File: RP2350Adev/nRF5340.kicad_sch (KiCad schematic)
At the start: 20 parts, among them J1 J-Link, J3 Conn_01x04, U2 nRF5340-QKxx, X1 32.768kHz, X2 32MHz

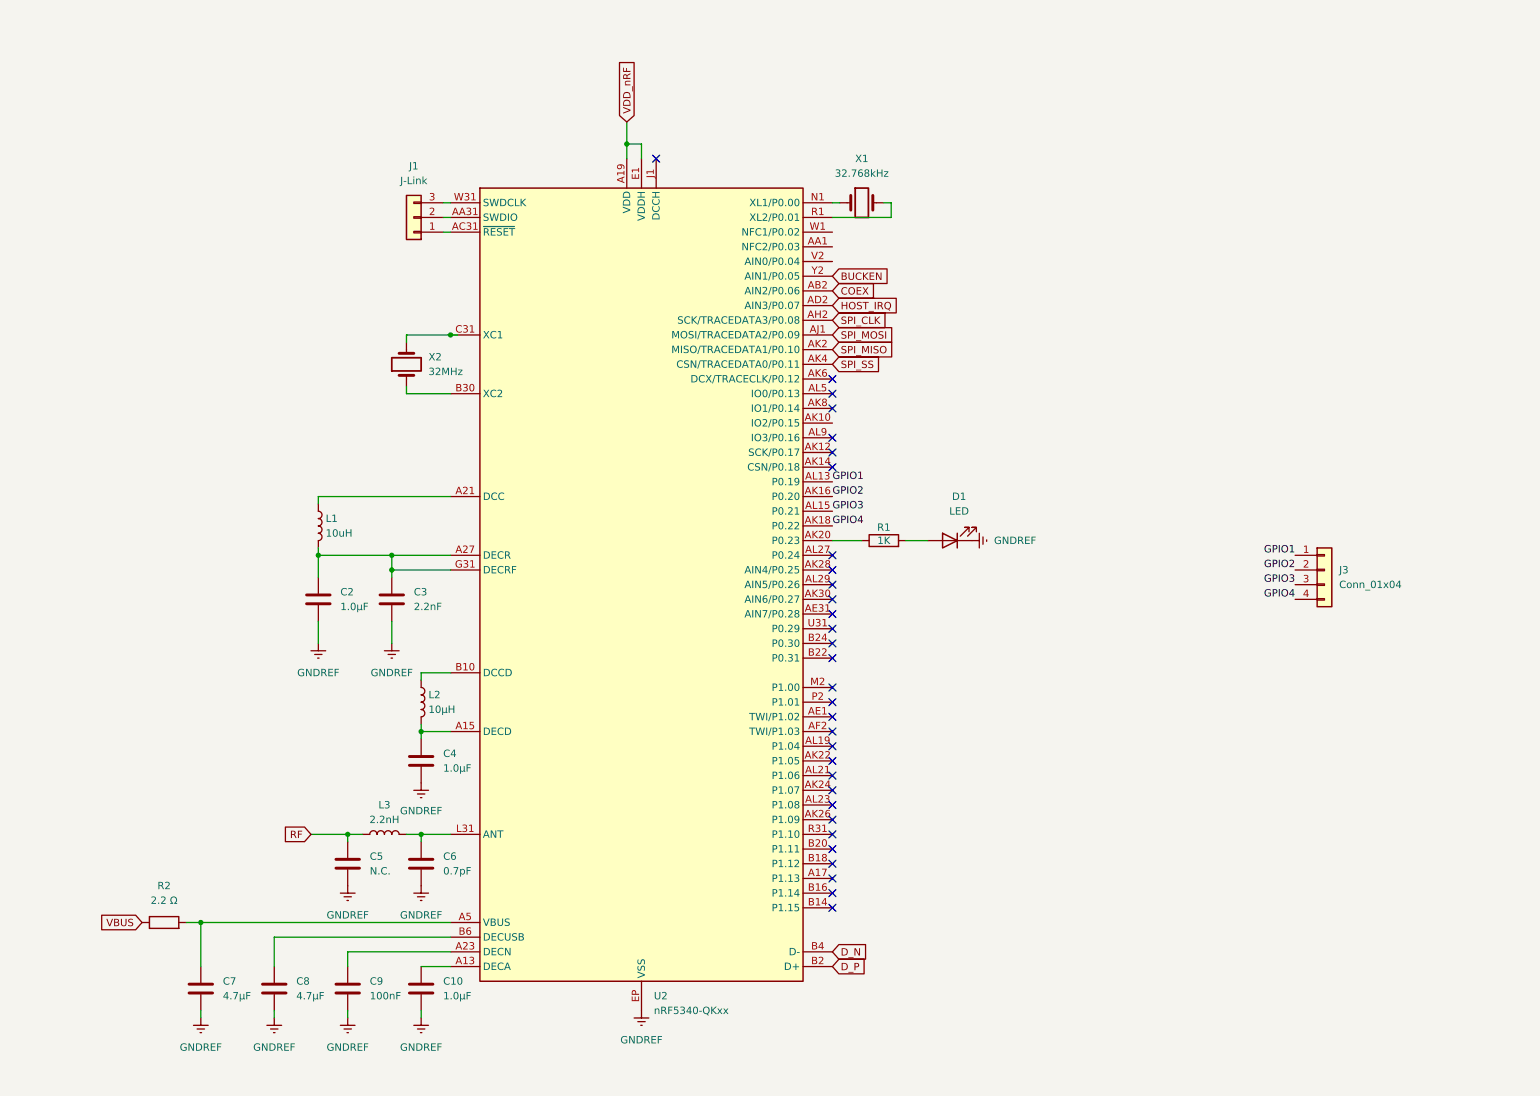
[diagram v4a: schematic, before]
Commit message: Updated nRF5340 with footprints and labels
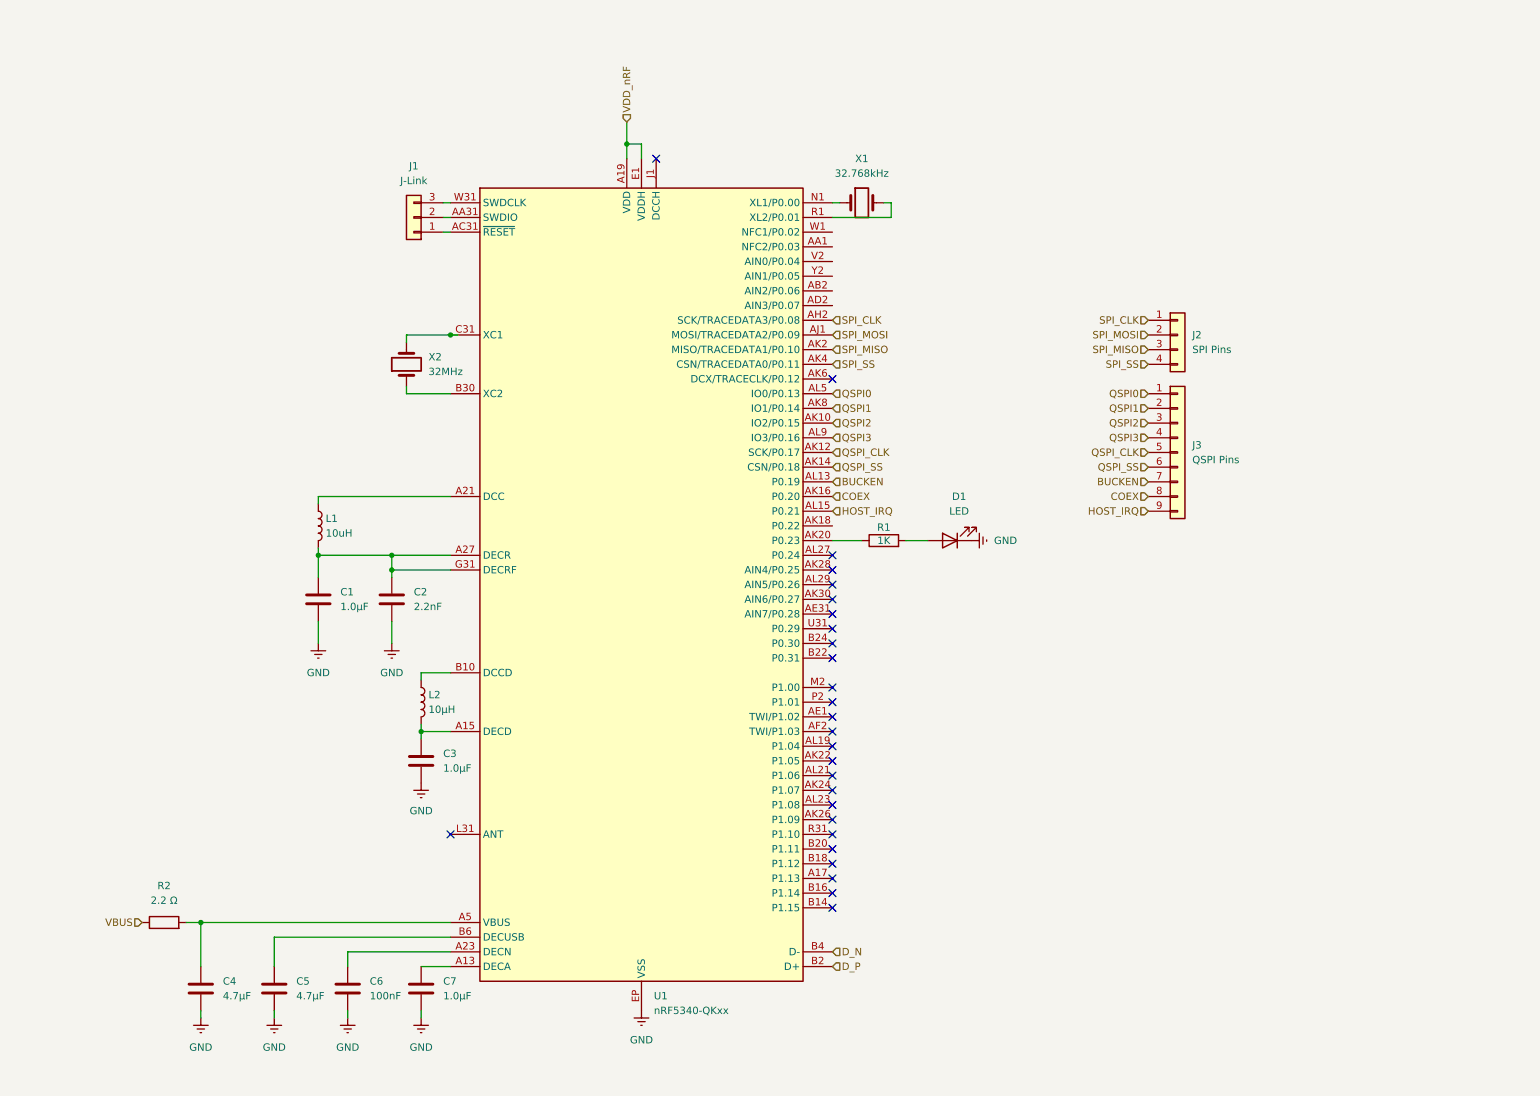
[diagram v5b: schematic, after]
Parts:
- removed C5: N.C., symbol Device:C
- removed C6: 0.7pF, symbol Device:C
- removed L3: 2.2nH, symbol Device:L
- added J3: QSPI Pins, Connector_PinHeader_2.54mm:PinHeader_1x09_P2.54mm_Vertical, symbol Connector_Generic:Conn_01x09
- C1: renamed from C2; footprint (none) -> Capacitor_SMD:C_0402_1005Metric
- C2: renamed from C3; footprint (none) -> Capacitor_SMD:C_0402_1005Metric
- C3: renamed from C4; footprint (none) -> Capacitor_SMD:C_0402_1005Metric
- C4: renamed from C7; footprint (none) -> Capacitor_SMD:C_0603_1608Metric
- C5: renamed from C8; footprint (none) -> Capacitor_SMD:C_0603_1608Metric
- C6: renamed from C9; footprint (none) -> Capacitor_SMD:C_0402_1005Metric
- C7: renamed from C10; footprint (none) -> Capacitor_SMD:C_0402_1005Metric
- D1: footprint (none) -> LED_SMD:LED_0805_2012Metric
- J1: footprint (none) -> Connector:FanPinHeader_1x03_P2.54mm_Vertical
- J2: renamed from J3; value Conn_01x04 -> SPI Pins; footprint (none) -> Connector:FanPinHeader_1x04_P2.54mm_Vertical
- L1, L2: footprint (none) -> Inductor_SMD:L_0603_1608Metric
- R2: footprint (none) -> Resistor_SMD:R_0402_1005Metric
- renumbered U2 to U1
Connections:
- net BUCKEN: now also U1.AL13 (P0.19), J3.7 (Pin_7); no longer U1.Y2 (AIN1/P0.05)
- net COEX: now also U1.AK16 (P0.20), J3.8 (Pin_8); no longer U1.AB2 (AIN2/P0.06)
- net HOST_IRQ: now also U1.AL15 (P0.21), J3.9 (Pin_9); no longer U1.AD2 (AIN3/P0.07)
- net SPI_CLK: now also J2.1 (Pin_1)
- net SPI_MISO: now also J2.3 (Pin_3)
- net SPI_MOSI: now also J2.2 (Pin_2)
- net SPI_SS: now also J2.4 (Pin_4)
- net QSPI2: now reaches U1.AK10 (IO2/P0.15)
- net QSPI2: now also J3.3 (Pin_3)
- net QSPI_CLK: now reaches U1.AK12 (SCK/P0.17)
- net QSPI_CLK: now also J3.5 (Pin_5)
- net QSPI_SS: now reaches U1.AK14 (CSN/P0.18)
- net QSPI_SS: now also J3.6 (Pin_6)
- net QSPI1: now reaches U1.AK8 (IO1/P0.14)
- net QSPI1: now also J3.2 (Pin_2)
- net QSPI0: now reaches U1.AL5 (IO0/P0.13)
- net QSPI0: now also J3.1 (Pin_1)
- net QSPI3: now reaches U1.AL9 (IO3/P0.16)
- net QSPI3: now also J3.4 (Pin_4)
- net GNDREF renamed GND
- removed net GPIO1: J2.1 (Pin_1), U1.AL13 (P0.19)
- removed net GPIO2: J2.2 (Pin_2), U1.AK16 (P0.20)
- removed net GPIO3: J2.3 (Pin_3), U1.AL15 (P0.21)
- net GPIO4: no longer names the net of U1.AK18 (P0.22)
- net GPIO4: no longer J2.4 (Pin_4)
- no-connect marks 31 -> 27
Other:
- moved on the sheet: J2

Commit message: Added UART and final footprints
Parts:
- added J4: UART Pins, Connector:FanPinHeader_1x03_P2.54mm_Vertical, symbol Connector_Generic:Conn_01x03
- L1, L2: footprint Inductor_SMD:L_0603_1608Metric -> Eclectronics:INDC1608X95N
- X1: footprint (none) -> Eclectronics:XTAL_CM9V-T1A-32.768KHZ-9PF-20PPM-TA-QC
- X2: footprint (none) -> Eclectronics:XTAL_ABM11W-32.0000MHZ-8-D1X-T3
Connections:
- net GND: now also J4.3 (Pin_3)
- net TX: now reaches U1.AK18 (P0.22)
- net TX: now also J4.1 (Pin_1)
- net at R1.1: now also U1.U31 (P0.29); no longer U1.AK20 (P0.23)
- new net RX: J4.2 (Pin_2), U1.AK20 (P0.23)
- no-connect marks 27 -> 32
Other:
- moved on the sheet: D1, R1
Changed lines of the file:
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@@
 	)
 	(no_connect
+		(at 154.94 104.14)
+	)
+	(no_connect
 		(at 124.46 35.56)
 	)
 	(no_connect
-		(at 154.94 116.84)
+		(at 154.94 53.34)
+	)
+	(no_connect
+		(at 154.94 48.26)
 	)
 	(no_connect
@@
 	)
 	(no_connect
-		(at 154.94 147.32)
+		(at 154.94 55.88)
 	)
 	(no_connect
-		(at 154.94 111.76)
+		(at 154.94 147.32)
 	)
 	(no_connect
-		(at 154.94 104.14)
+		(at 154.94 111.76)
 	)
 	(no_connect
@@
 	)
 	(no_connect
+		(at 154.94 60.96)
+	)
+	(no_connect
 		(at 154.94 114.3)
 	)
@@
 	)
 	(no_connect
+		(at 154.94 58.42)
+	)
+	(no_connect
 		(at 154.94 154.94)
 	)
@@
 	)
 	(no_connect
+		(at 154.94 50.8)
+	)
+	(no_connect
 		(at 154.94 162.56)
 	)
@@
 	(wire
 		(pts
-			(xy 154.94 101.6) (xy 160.02 101.6)
-		)
-		(stroke
-			(width 0)
-			(type default)
-		)
-	)
-	(wire
-		(pts
-			(xy 167.64 101.6) (xy 171.45 101.6)
+			(xy 162.56 116.84) (xy 166.37 116.84)
 		)
 		(stroke
@@
 		)
 	)
+	(hierarchical_label "TX"
+		(shape input)
+		(at 154.94 99.06 0)
+		(effects
+			(font
+				(size 1.27 1.27)
+			)
+			(justify left)
+		)
+	)
 	(hierarchical_label "COEX"
 		(shape input)
@@
 		)
 	)
+	(hierarchical_label "RX"
+		(shape input)
+		(at 154.94 101.6 0)
+		(effects
+			(font
+				(size 1.27 1.27)
+			)
+			(justify left)
+		)
+	)
+	(hierarchical_label "TX"
+		(shape input)
+		(at 209.55 106.68 180)
+		(effects
+			(font
+				(size 1.27 1.27)
+			)
+			(justify right)
+		)
+	)
 	(hierarchical_label "QSPI0"
 		(shape input)
@@
 		)
 	)
+	(hierarchical_label "RX"
+		(shape input)
+		(at 209.55 109.22 180)
+		(effects
+			(font
+				(size 1.27 1.27)
+			)
+			(justify right)
+		)
+	)
 	(hierarchical_label "SPI_SS"
 		(shape input)
@@
 			)
 		)
-		(property "Footprint" ""
+		(property "Footprint" "Eclectronics:XTAL_ABM11W-32.0000MHZ-8-D1X-T3"
 			(at 81.28 71.12 0)
 			(effects
@@
 	(symbol
 		(lib_id "Device:R")
-		(at 163.83 101.6 90)
+		(at 158.75 116.84 90)
 		(unit 1)
 		(exclude_from_sim no)
@@
 		(dnp no)
 		(property "Reference" "R1"
-			(at 163.83 99.314 90)
+			(at 158.75 114.554 90)
 			(effects
 				(font
@@
 		)
 		(property "Value" "1K"
-			(at 163.83 101.6 90)
+			(at 158.75 116.84 90)
 			(effects
 				(font
@@
 		)
 		(property "Footprint" "Resistor_SMD:R_0402_1005Metric"
-			(at 163.83 103.378 90)
+			(at 158.75 118.618 90)
 			(effects
 				(font
@@
 		)
 		(property "Datasheet" "~"
-			(at 163.83 101.6 0)
+			(at 158.75 116.84 0)
 			(effects
 				(font
@@
 		)
 		(property "Description" ""
-			(at 163.83 101.6 0)
+			(at 158.75 116.84 0)
 			(effects
 				(font
@@
 			)
 		)
-		(property "Footprint" "Inductor_SMD:L_0603_1608Metric"
+		(property "Footprint" "Eclectronics:INDC1608X95N"
 			(at 83.82 129.54 0)
 			(effects
@@
 	(symbol
 		(lib_id "power:GNDREF")
-		(at 179.07 101.6 90)
+		(at 209.55 111.76 270)
+		(unit 1)
+		(exclude_from_sim no)
+		(in_bom yes)
+		(on_board yes)
+		(dnp no)
+		(fields_autoplaced yes)
+		(property "Reference" "#PWR010"
+			(at 203.2 111.76 0)
+			(effects
+				(font
+					(size 1.27 1.27)
+				)
+				(hide yes)
+			)
+		)
+		(property "Value" "GND"
+			(at 205.74 111.7599 90)
+			(effects
+				(font
+					(size 1.27 1.27)
+				)
+				(justify right)
+			)
+		)
+		(property "Footprint" ""
+			(at 209.55 111.76 0)
+			(effects
+				(font
+					(size 1.27 1.27)
+				)
+				(hide yes)
+			)
+		)
+		(property "Datasheet" ""
+			(at 209.55 111.76 0)
+			(effects
+				(font
+					(size 1.27 1.27)
+				)
+				(hide yes)
+			)
+		)
+		(property "Description" "Power symbol creates a global label with name \"GNDREF\" , reference supply ground"
+			(at 209.55 111.76 0)
+			(effects
+				(font
+					(size 1.27 1.27)
+				)
+				(hide yes)
+			)
+		)
+		(pin "1"
+		)
+		(instances
+			(project "nRF5340"
+				(path "/f5f40e54-af19-4cbb-b665-07a5a1b1caaa"
+					(reference "#PWR010")
+					(unit 1)
+				)
+			)
+		)
+	)
+	(symbol
+		(lib_id "power:GNDREF")
+		(at 173.99 116.84 90)
 		(unit 1)
 		(exclude_from_sim no)
@@
 		(fields_autoplaced yes)
 		(property "Reference" "#PWR01"
-			(at 185.42 101.6 0)
+			(at 180.34 116.84 0)
 			(effects
 				(font
@@
 		)
 		(property "Value" "GND"
-			(at 182.88 101.5999 90)
+			(at 177.8 116.8399 90)
 			(effects
 				(font
@@
 		)
 		(property "Footprint" ""
-			(at 179.07 101.6 0)
+			(at 173.99 116.84 0)
 			(effects
 				(font
@@
 		)
 		(property "Datasheet" ""
-			(at 179.07 101.6 0)
+			(at 173.99 116.84 0)
 			(effects
 				(font
@@
 		)
 		(property "Description" "Power symbol creates a global label with name \"GNDREF\" , reference supply ground"
-			(at 179.07 101.6 0)
+			(at 173.99 116.84 0)
 			(effects
 				(font
@@
 			)
 		)
-		(property "Footprint" "Inductor_SMD:L_0603_1608Metric"
+		(property "Footprint" "Eclectronics:INDC1608X95N"
 			(at 66.04 99.06 0)
 			(effects
@@
 	(symbol
 		(lib_id "Device:LED")
-		(at 175.26 101.6 180)
+		(at 170.18 116.84 180)
 		(unit 1)
 		(exclude_from_sim no)
@@
 		(fields_autoplaced yes)
 		(property "Reference" "D1"
-			(at 176.8475 93.98 0)
+			(at 171.7675 109.22 0)
 			(effects
 				(font
@@
 		)
 		(property "Value" "LED"
-			(at 176.8475 96.52 0)
+			(at 171.7675 111.76 0)
 			(effects
 				(font
@@
 		)
 		(property "Footprint" "LED_SMD:LED_0805_2012Metric"
-			(at 175.26 101.6 0)
+			(at 170.18 116.84 0)
 			(effects
 				(font
@@
 		)
 		(property "Datasheet" "~"
-			(at 175.26 101.6 0)
+			(at 170.18 116.84 0)
 			(effects
 				(font
@@
 		)
 		(property "Description" "Light emitting diode"
-			(at 175.26 101.6 0)
+			(at 170.18 116.84 0)
 			(effects
 				(font
@@
 		)
 		(property "Sim.Pins" "1=K 2=A"
-			(at 175.26 101.6 0)
+			(at 170.18 116.84 0)
 			(effects
 				(font
@@
 	)
 	(symbol
+		(lib_id "Connector_Generic:Conn_01x03")
+		(at 214.63 109.22 0)
+		(unit 1)
+		(exclude_from_sim no)
+		(in_bom yes)
+		(on_board yes)
+		(dnp no)
+		(fields_autoplaced yes)
+		(property "Reference" "J4"
+			(at 217.17 107.9499 0)
+			(effects
+				(font
+					(size 1.27 1.27)
+				)
+				(justify left)
+			)
+		)
+		(property "Value" "UART Pins"
+			(at 217.17 110.4899 0)
+			(effects
+				(font
+					(size 1.27 1.27)
+				)
+				(justify left)
+			)
+		)
+		(property "Footprint" "Connector:FanPinHeader_1x03_P2.54mm_Vertical"
+			(at 214.63 109.22 0)
+			(effects
+				(font
+					(size 1.27 1.27)
+				)
+				(hide yes)
+			)
+		)
+		(property "Datasheet" "~"
+			(at 214.63 109.22 0)
+			(effects
+				(font
+					(size 1.27 1.27)
+				)
+				(hide yes)
+			)
+		)
+		(property "Description" "Generic connector, single row, 01x03, script generated (kicad-library-utils/schlib/autogen/connector/)"
+			(at 214.63 109.22 0)
+			(effects
+				(font
+					(size 1.27 1.27)
+				)
+				(hide yes)
+			)
+		)
+		(pin "1"
+		)
+		(pin "2"
+		)
+		(pin "3"
+		)
+		(instances
+			(project ""
+				(path "/f5f40e54-af19-4cbb-b665-07a5a1b1caaa"
+					(reference "J4")
+					(unit 1)
+				)
+			)
+		)
+	)
+	(symbol
 		(lib_id "Device:Crystal")
 		(at 160.02 43.18 0)
@@
 			)
 		)
-		(property "Footprint" ""
+		(property "Footprint" "Eclectronics:XTAL_CM9V-T1A-32.768KHZ-9PF-20PPM-TA-QC"
 			(at 160.02 43.18 0)
 			(effects

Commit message: Combine subsheets
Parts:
- renumbered C4 to C1, C5 to C2, C1 to C3, C6 to C4, C2 to C5, C3 to C6, R2 to R1, R1 to R2, X2 to X1, X1 to X2
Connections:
- net MUX2_S: now reaches U1.AK24 (P1.07)
- net MUX1_S1: now reaches U1.AK26 (P1.09)
- net MUX2_OE: now reaches U1.AL23 (P1.08)
- net IOVDD_EN: now reaches U1.AL27 (P0.24)
- net MUX1_S0: now reaches U1.R31 (P1.10)
- no-connect marks 32 -> 27

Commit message: Updated
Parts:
- added C10, C11, C12, C13, C3, C4, C5, C6: 100nF, Capacitor_SMD:C_0402_1005Metric, symbol Device:C
- added C7, C8: 1.0µF, Capacitor_SMD:C_0402_1005Metric, symbol Device:C
- J1, J4: footprint Connector:FanPinHeader_1x03_P2.54mm_Vertical -> Connector_PinHeader_2.54mm:PinHeader_1x03_P2.54mm_Vertical
- J2: footprint Connector:FanPinHeader_1x04_P2.54mm_Vertical -> Connector_PinHeader_2.54mm:PinHeader_1x04_P2.54mm_Vertical
- renumbered C3 to C1, C1 to C14, C2 to C15, C4 to C16, C7 to C17, C5 to C2, C6 to C9, R2 to R1, R1 to R2, X2 to X1, X1 to X2
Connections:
- net COEX: no longer U1.AK16 (P0.20)
- net GND: now also C10.1, C11.1, C12.1, C13.1, C3.1, C4.1, C5.1, C6.1, C7.1, C8.1
- net RX: now also U1.B24 (P0.30); no longer U1.AK20 (P0.23)
- net TX: now also U1.B22 (P0.31); no longer U1.AK18 (P0.22)
- net VDD_nRF: now also C10.2, C11.2, C12.2, C13.2, C3.2, C4.2, C5.2, C6.2, C7.2, C8.2
- no-connect marks 27 -> 28
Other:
- moved on the sheet: C1, C14, C15, C16, C17, C2, C9, D1, J1, L1, L2, R1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
